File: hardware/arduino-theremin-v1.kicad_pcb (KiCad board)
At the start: 2 copper layers, 71.1 x 53.3 mm, 15 parts, among them U1 ARDUINO-UNO-SHIELD

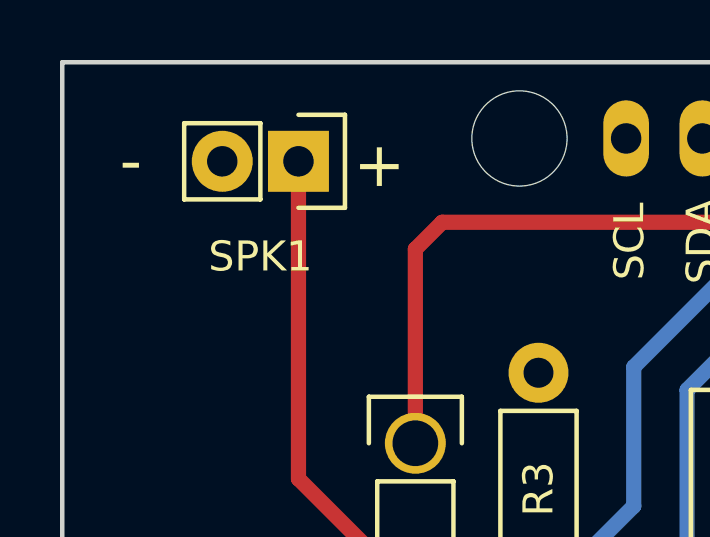
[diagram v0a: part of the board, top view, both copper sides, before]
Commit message: Ported Arduino Theremin to use Wickerlib.
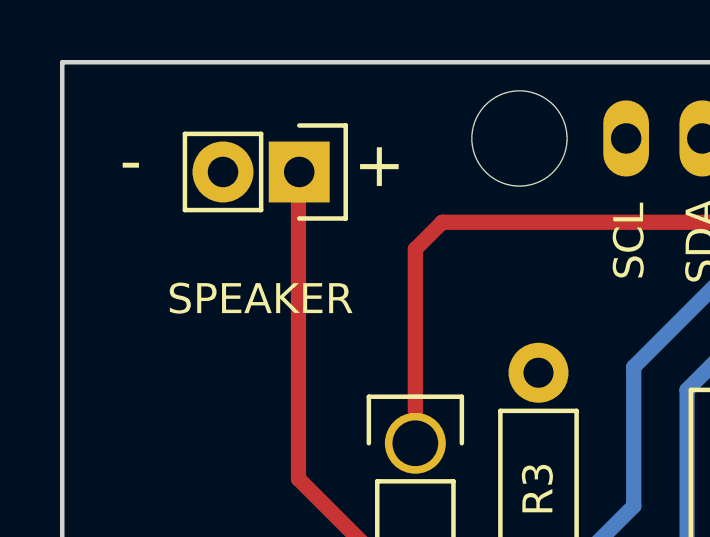
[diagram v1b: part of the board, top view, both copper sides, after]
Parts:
- removed SPK1: SPEAKER-8OHM-23MM-ROUND-2PIN, Wickerlib:Pin_Header_Straight_1x02
- added SPEAKER: 8 OHM, Wickerlib:OSTVN02A150, F.Cu at (95.5, 68.4)
- S1: value RECORD-OFF-PLAYBACK -> 100SP3 ON-OFF-ON
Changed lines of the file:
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@@
     (links 27)
     (no_connects 0)
-    (area 84.211888 53.457286 178.510001 123.265001)
+    (area 87.554999 64.694999 158.825001 118.185001)
     (thickness 1.6)
     (drawings 38)
@@
     (39 F.Mask user)
     (44 Edge.Cuts user)
+    (46 B.CrtYd user)
+    (47 F.CrtYd user)
+    (48 B.Fab user)
+    (49 F.Fab user)
   )
   (setup
-    (last_trace_width 0.508)
+    (last_trace_width 0.254)
     (user_trace_width 0.1524)
     (user_trace_width 0.254)
@@
       (effects (font (size 1 1) (thickness 0.15)))
     )
-    (fp_text value RECORD-OFF-PLAYBACK (at 0 -3.1 270) (layer F.Fab)
+    (fp_text value "100SP3 ON-OFF-ON" (at 0 -3.1 270) (layer F.Fab)
       (effects (font (size 1 1) (thickness 0.15)))
     )
@@
     (pad 3 thru_hole circle (at 0 9.398 270) (size 2.54 2.54) (drill 2.032) (layers *.Cu *.Mask F.SilkS)
       (net 8 /D9_BTN_RECORD))
-  )
-  (module Wickerlib:Pin_Header_Straight_1x02 (layer F.Cu)
-    (at 95.504 68.072 270)
-    (descr "Through hole pin header")
-    (tags "pin header")
-    (fp_text reference SPK1 (at 3.175 1.27 360) (layer F.SilkS)
-      (effects (font (size 1 1) (thickness 0.15)))
-    )
-    (fp_text value SPEAKER-8OHM-23MM-ROUND-2PIN (at 0 -3.1 270) (layer F.Fab)
-      (effects (font (size 1 1) (thickness 0.15)))
-    )
-    (fp_line (start 1.27 1.27) (end 1.27 3.81) (layer F.SilkS) (width 0.15))
-    (fp_line (start 1.55 -1.55) (end 1.55 0) (layer F.SilkS) (width 0.15))
-    (fp_line (start -1.75 -1.75) (end -1.75 4.3) (layer F.CrtYd) (width 0.05))
-    (fp_line (start 1.75 -1.75) (end 1.75 4.3) (layer F.CrtYd) (width 0.05))
-    (fp_line (start -1.75 -1.75) (end 1.75 -1.75) (layer F.CrtYd) (width 0.05))
-    (fp_line (start -1.75 4.3) (end 1.75 4.3) (layer F.CrtYd) (width 0.05))
-    (fp_line (start 1.27 1.27) (end -1.27 1.27) (layer F.SilkS) (width 0.15))
-    (fp_line (start -1.55 0) (end -1.55 -1.55) (layer F.SilkS) (width 0.15))
-    (fp_line (start -1.55 -1.55) (end 1.55 -1.55) (layer F.SilkS) (width 0.15))
-    (fp_line (start -1.27 1.27) (end -1.27 3.81) (layer F.SilkS) (width 0.15))
-    (fp_line (start -1.27 3.81) (end 1.27 3.81) (layer F.SilkS) (width 0.15))
-    (pad 1 thru_hole rect (at 0 0 270) (size 2.032 2.032) (drill 1.016) (layers *.Cu *.Mask F.SilkS)
-      (net 9 "Net-(RV1-Pad2)"))
-    (pad 2 thru_hole oval (at 0 2.54 270) (size 2.032 2.032) (drill 1.016) (layers *.Cu *.Mask F.SilkS)
-      (net 2 GND))
-    (model Pin_Headers.3dshapes/Pin_Header_Straight_1x02.wrl
-      (at (xyz 0 -0.05 0))
-      (scale (xyz 1 1 1))
-      (rotate (xyz 0 0 90))
-    )
   )
   (module Wickerlib:ARDU-UNOSHIELD locked (layer F.Cu)
@@
     (pad NC thru_hole oval (at 27.94 -2.54 90) (size 2.54 1.524) (drill 1.016) (layers *.Cu *.Mask F.SilkS))
   )
+  (module Wickerlib:OSTVN02A150 (layer F.Cu)
+    (at 95.5294 68.4276 270)
+    (descr "Through hole pin header")
+    (tags "pin header")
+    (fp_text reference SPEAKER (at 4.2418 1.2954 360) (layer F.SilkS)
+      (effects (font (size 1 1) (thickness 0.15)))
+    )
+    (fp_text value "8 OHM" (at 0 -3.1 270) (layer F.Fab)
+      (effects (font (size 1 1) (thickness 0.15)))
+    )
+    (fp_line (start 1.27 1.27) (end 1.27 3.81) (layer F.SilkS) (width 0.15))
+    (fp_line (start 1.55 -1.55) (end 1.55 0) (layer F.SilkS) (width 0.15))
+    (fp_line (start -3.3 -1.75) (end -3.3 4.3) (layer F.CrtYd) (width 0.05))
+    (fp_line (start 3.3 -1.75) (end 3.3 4.3) (layer F.CrtYd) (width 0.05))
+    (fp_line (start -3.3 -1.75) (end 3.3 -1.74244) (layer F.CrtYd) (width 0.05))
+    (fp_line (start -3.3 4.3) (end 3.3 4.3) (layer F.CrtYd) (width 0.05))
+    (fp_line (start 1.27 1.27) (end -1.27 1.27) (layer F.SilkS) (width 0.15))
+    (fp_line (start -1.55 0) (end -1.55 -1.55) (layer F.SilkS) (width 0.15))
+    (fp_line (start -1.55 -1.55) (end 1.55 -1.55) (layer F.SilkS) (width 0.15))
+    (fp_line (start -1.27 1.27) (end -1.27 3.81) (layer F.SilkS) (width 0.15))
+    (fp_line (start -1.27 3.81) (end 1.27 3.81) (layer F.SilkS) (width 0.15))
+    (pad 1 thru_hole rect (at 0 0 270) (size 2.032 2.032) (drill 1.016) (layers *.Cu *.Mask F.SilkS)
+      (net 9 "Net-(RV1-Pad2)"))
+    (pad 2 thru_hole oval (at 0 2.54 270) (size 2.032 2.032) (drill 1.016) (layers *.Cu *.Mask F.SilkS)
+      (net 2 GND))
+    (model Pin_Headers.3dshapes/Pin_Header_Straight_1x02.wrl
+      (at (xyz 0 -0.05 0))
+      (scale (xyz 1 1 1))
+      (rotate (xyz 0 0 90))
+    )
+  )
   (gr_text RECORD (at 91.821 99.187 90) (layer F.SilkS)

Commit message: Updated board file to match correct names for D8 and D9 PLAYBACK and RECORD. All done.
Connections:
- net /D8_BTN_PLAYBACK renamed /D8_BTN_RECORD
- net /D9_BTN_RECORD renamed /D9_BTN_PLAYBACK
